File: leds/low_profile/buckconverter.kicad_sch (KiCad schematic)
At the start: 15 parts, among them U2 LM66100DCK, U3 TPS54202DDC, U6 TVS0500DRV

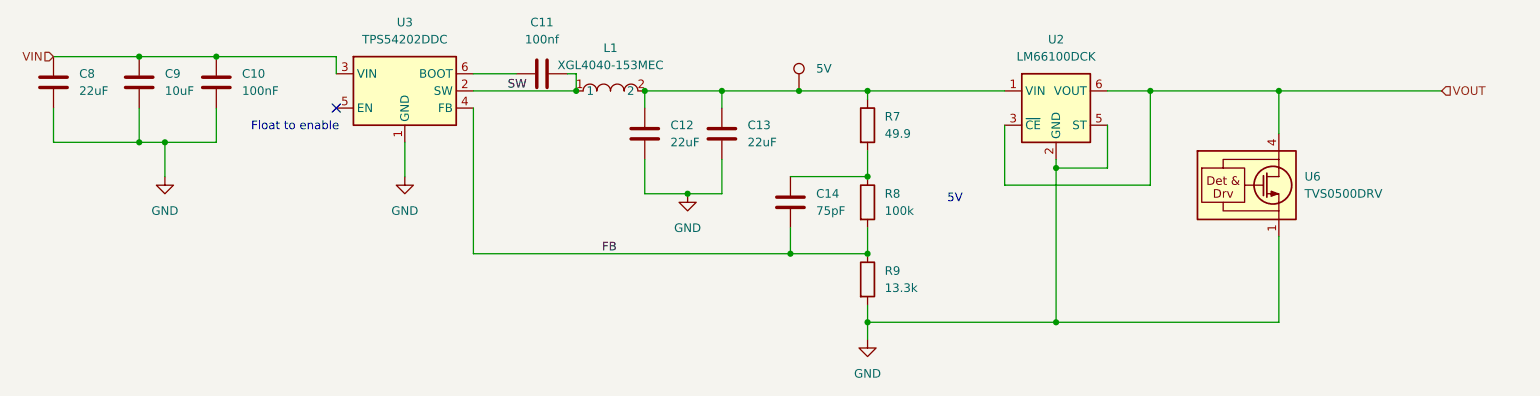
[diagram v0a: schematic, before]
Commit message: Low profile LED controller
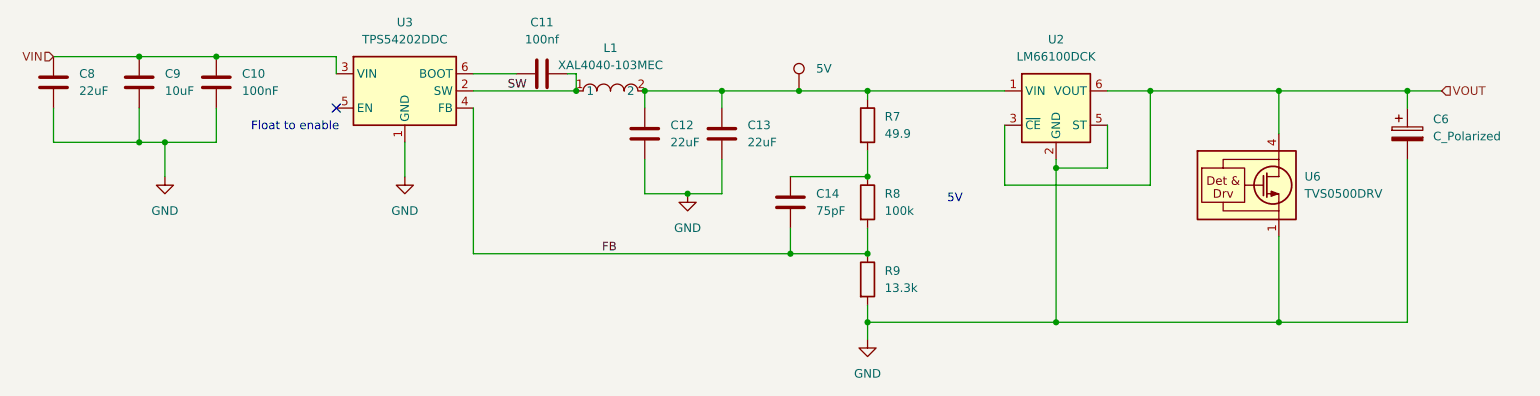
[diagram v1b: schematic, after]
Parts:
- removed L1: XGL4040-153MEC, easyeda2kicad:IND-SMD_L4.0-W4.0_XAL4040-103, symbol easyeda2kicad:XGL4040-153MEC
- added C6: C_Polarized, Capacitor_SMD:CP_Elec_8x11.9, symbol Device:C_Polarized
- added L1: XAL4040-103MEC, easyeda2kicad:IND-SMD_L4.0-W4.0-A, symbol easyeda2kicad:XAL4040-103MEC
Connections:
- net GND: now also C6.2
- net SW: now also L1.1
- net VOUT: now also C6.1
- net at C12.1, C13.1, R7.1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: now also L1.2
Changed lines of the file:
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@@
+	)
+	(junction
+		(at 204.47 67.31)
+		(diameter 0)
+		(color 0 0 0 0)
 	)
 	(junction
@@
 	)
 	(junction
+		(at 223.52 33.02)
+		(diameter 0)
+		(color 0 0 0 0)
+	)
+	(junction
 		(at 35.56 40.64)
 		(diameter 0)
@@
 	)
 	(junction
+		(at 110.49 33.02)
+		(diameter 0)
+		(color 0 0 0 0)
+	)
+	(junction
 		(at 46.99 27.94)
 		(diameter 0)
@@
 	)
 	(junction
+		(at 100.33 33.02)
+		(diameter 0)
+		(color 0 0 0 0)
+	)
+	(junction
 		(at 143.51 67.31)
 		(diameter 0)
@@
 	)
 	(junction
-		(at 100.33 33.02)
-		(diameter 0)
-		(color 0 0 0 0)
-	)
-	(junction
 		(at 171.45 67.31)
 		(diameter 0)
@@
 		(color 0 0 0 0)
 	)
-	(junction
-		(at 110.49 33.02)
-		(diameter 0)
-		(color 0 0 0 0)
-	)
 	(no_connect
 		(at 64.77 35.56)
@@
 	(wire
 		(pts
+			(xy 223.52 67.31) (xy 204.47 67.31)
+		)
+		(stroke
+			(width 0)
+			(type default)
+		)
+	)
+	(wire
+		(pts
 			(xy 133.35 33.02) (xy 143.51 33.02)
 		)
@@
 	(wire
 		(pts
-			(xy 204.47 33.02) (xy 228.6 33.02)
+			(xy 204.47 33.02) (xy 223.52 33.02)
 		)
 		(stroke
@@
 	(wire
 		(pts
+			(xy 223.52 33.02) (xy 228.6 33.02)
+		)
+		(stroke
+			(width 0)
+			(type default)
+		)
+	)
+	(wire
+		(pts
 			(xy 121.92 33.02) (xy 121.92 35.56)
 		)
@@
 	(wire
 		(pts
+			(xy 223.52 43.18) (xy 223.52 67.31)
+		)
+		(stroke
+			(width 0)
+			(type default)
+		)
+	)
+	(wire
+		(pts
 			(xy 185.42 33.02) (xy 185.42 46.99)
 		)
@@
 		(pts
 			(xy 22.86 27.94) (xy 35.56 27.94)
+		)
+		(stroke
+			(width 0)
+			(type default)
+		)
+	)
+	(wire
+		(pts
+			(xy 223.52 35.56) (xy 223.52 33.02)
 		)
 		(stroke
@@
 	)
 	(symbol
+		(lib_id "Device:C_Polarized")
+		(at 223.52 39.37 0)
+		(unit 1)
+		(exclude_from_sim no)
+		(in_bom yes)
+		(on_board yes)
+		(dnp no)
+		(fields_autoplaced yes)
+		(property "Reference" "C6"
+			(at 227.33 37.2109 0)
+			(effects
+				(font
+					(size 1.27 1.27)
+				)
+				(justify left)
+			)
+		)
+		(property "Value" "C_Polarized"
+			(at 227.33 39.7509 0)
+			(effects
+				(font
+					(size 1.27 1.27)
+				)
+				(justify left)
+			)
+		)
+		(property "Footprint" "Capacitor_SMD:CP_Elec_8x11.9"
+			(at 224.4852 43.18 0)
+			(effects
+				(font
+					(size 1.27 1.27)
+				)
+				(hide yes)
+			)
+		)
+		(property "Datasheet" "~"
+			(at 223.52 39.37 0)
+			(effects
+				(font
+					(size 1.27 1.27)
+				)
+				(hide yes)
+			)
+		)
+		(property "Description" "Polarized capacitor"
+			(at 223.52 39.37 0)
+			(effects
+				(font
+					(size 1.27 1.27)
+				)
+				(hide yes)
+			)
+		)
+		(property "Label" ""
+			(at 223.52 39.37 0)
+			(effects
+				(font
+					(size 1.27 1.27)
+				)
+				(hide yes)
+			)
+		)
+		(property "LCSC Part" "C542295"
+			(at 223.52 39.37 0)
+			(effects
+				(font
+					(size 1.27 1.27)
+				)
+				(hide yes)
+			)
+		)
+		(pin "2"
+		)
+		(pin "1"
+		)
+		(instances
+			(project "low_profile"
+				(path "/48ddfdd8-68fa-4e63-aa18-bc113cdf8cfa/aa9739d0-05d8-4c74-a4fd-846c263eed0b"
+					(reference "C6")
+					(unit 1)
+				)
+			)
+		)
+	)
+	(symbol
 		(lib_id "Regulator_Switching:TPS54202DDC")
 		(at 74.93 33.02 0)
@@
 	)
 	(symbol
-		(lib_id "easyeda2kicad:XGL4040-153MEC")
+		(lib_id "easyeda2kicad:XAL4040-103MEC")
 		(at 105.41 33.02 0)
 		(unit 1)
@@
 			)
 		)
-		(property "Value" "XGL4040-153MEC"
+		(property "Value" "XAL4040-103MEC"
 			(at 105.41 29.21 0)
 			(effects
@@
 			)
 		)
-		(property "Footprint" "easyeda2kicad:IND-SMD_L4.0-W4.0_XAL4040-103"
+		(property "Footprint" "easyeda2kicad:IND-SMD_L4.0-W4.0-A"
 			(at 105.41 40.64 0)
 			(effects
@@
 			)
 		)
-		(property "LCSC Part" "C3911667"
+		(property "LCSC Part" "C5144883"
 			(at 105.41 43.18 0)
 			(effects
@@
 		)
 		(instances
-			(project "hi_amp"
+			(project ""
 				(path "/48ddfdd8-68fa-4e63-aa18-bc113cdf8cfa/aa9739d0-05d8-4c74-a4fd-846c263eed0b"
 					(reference "L1")
